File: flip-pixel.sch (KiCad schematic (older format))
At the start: 8 parts, among them Q1 Q_NMOS_DGS, U1 LM2665M6

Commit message: Added charge pump for gate driving, MicroController, and Power Connector
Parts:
- added J?: Barrel-Jack, symbol Custom-Symbols:Barrel-Jack
- added U?: ESP32_DevBoard, symbol Custom-Symbols:ESP32_DevBoard
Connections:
- net labels added: +10V, +5V, Col1H, Col1L, Col2H, Col2L, Col3H, Col3L, Col4H, Col4L, Col5H, Col5L, Row1H, Row1L, Row2H, Row2L, Row3H, Row3L, Row4H, Row4L, Row5H, Row5L
- wire segments 84 -> 157
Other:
- note added: "(AC -> DC Wall Adapter)\nExpects 5V, 2A max rating"
- note added: "Mates With:"
- moved on the sheet: C1, C2, C3, D1, R1, R2, U1

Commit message: Started work on layout
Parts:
- removed Q1: Q_NMOS_DGS, symbol Device:Q_NMOS_DGS
- added D52, D53: LED_Green, LED_SMD:LED_0805_2012Metric_Pad1.15x1.40mm_HandSolder, symbol Custom-Symbols:LED_Green
- added Q1: DMN62D0U-7, Package_TO_SOT_SMD:SOT-23, symbol Custom-Symbols:DMN62D0U-7
- added R23, R24: R, Resistor_SMD:R_0805_2012Metric, symbol Device:R
- C1, C2, C3: footprint (none) -> Capacitor_SMD:C_0805_2012Metric
- R1, R2: footprint (none) -> Resistor_SMD:R_0805_2012Metric
- gave numbers to parts that had none: 2
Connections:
- wire segments 157 -> 163
- no-connect marks 0 -> 10
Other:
- note added: "enable signal enables the high current\noperation of the pixel matrix by\ndriving the charge pump's\nshutdown pin low"
- note removed: "Signal enables the high current\noperation of the pixel matrix by\ndriving the charge pump's\nshutdown pin low"
- moved on the sheet: R1, U2

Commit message: Traces Routed for Charge Pump
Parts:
- J1: footprint (none) -> Connector_BarrelJack:BarrelJack_Horizontal
- U2: footprint (none) -> Custom-Footprints:DIP-38_900_ELL
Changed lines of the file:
@@
 F 0 "U2" H 1650 5465 50  0000 C CNN
 F 1 "ESP32_DevBoard" H 1650 5374 50  0000 C CNN
-F 2 "" H 2000 5450 50  0001 C CNN
+F 2 "Custom-Footprints:DIP-38_900_ELL" H 2000 5450 50  0001 C CNN
 F 3 "http://wiki.ai-thinker.com/_media/esp32/docs/nodemcu-32s_product_specification.pdf" H 2000 5450 50  0001 C CNN
 F 4 "https://www.espressif.com/sites/default/files/documentation/esp32-wroom-32_datasheet_en.pdf" H 1650 4450 50  0001 C CNN "ChipDatasheet"
@@
 F 0 "J1" H 1100 1550 50  0000 C CNN
 F 1 "Barrel-Jack" H 1400 1550 50  0000 C CNN
-F 2 "" H 1700 1550 50  0001 C CNN
+F 2 "Connector_BarrelJack:BarrelJack_Horizontal" H 1700 1550 50  0001 C CNN
 F 3 "https://www.cuidevices.com/product/resource/pj-102b.pdf" H 1700 1550 50  0001 C CNN
 F 4 "Digikey" H 950 2000 50  0001 C CNN "Vendor"

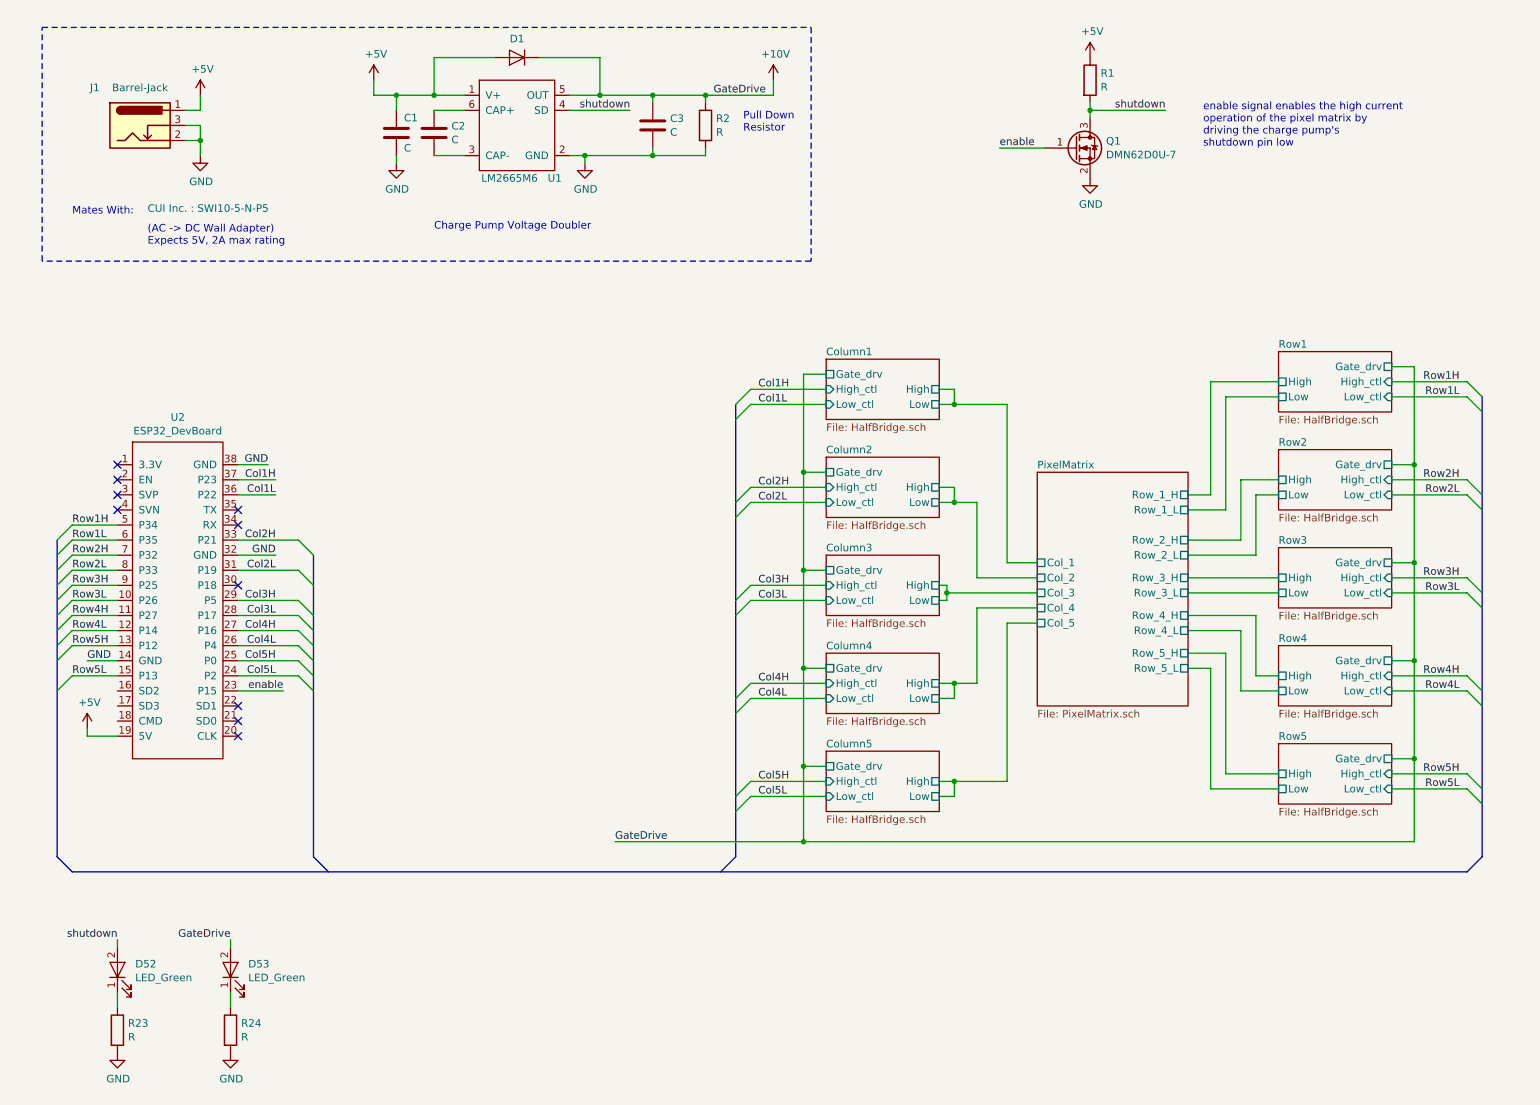
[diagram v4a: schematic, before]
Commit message: Added Current Sensor to Schematic
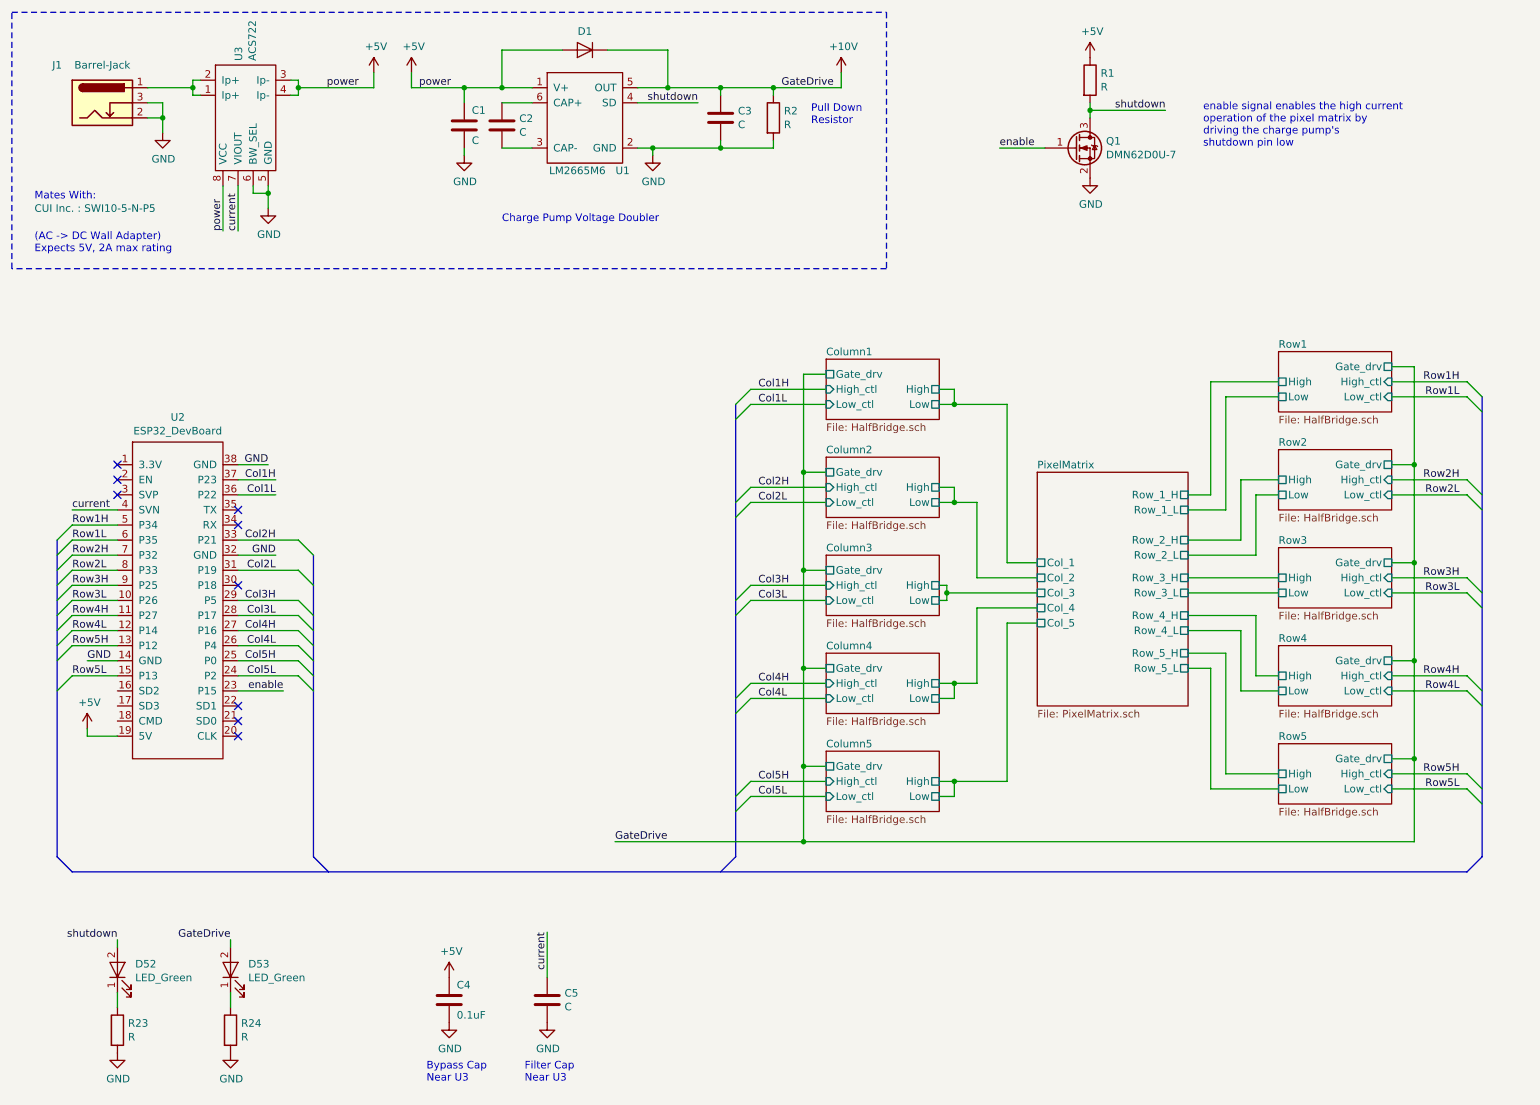
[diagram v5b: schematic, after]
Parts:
- added C4: 0.1uF, Capacitor_SMD:C_0805_2012Metric, symbol Device:C
- added C5: C, Capacitor_SMD:C_0805_2012Metric, symbol Device:C
- added U3: ACS722, Custom-Footprints:SO-8_3.9x4.9mm_P1.27mm, symbol Custom-Symbols:ACS722
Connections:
- net +5V: now also C4.1, U3.3 (Ip-), U3.4 (Ip-), U3.8 (VCC); no longer J1.1
- net GND: now also C4.2, C5.2, U3.5 (GND), U3.6 (BW_SEL)
- net current: now reaches U2.4 (SVN)
- net current: now also C5.1, U3.7 (VIOUT)
- new net: J1.1, U3.1 (Ip+), U3.2 (Ip+)
- no-connect marks 10 -> 9
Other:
- note added: "Bypass Cap\nNear U3"
- note added: "Filter Cap\nNear U3"
- moved on the sheet: C1, C2, C3, D1, J1, R2, U1

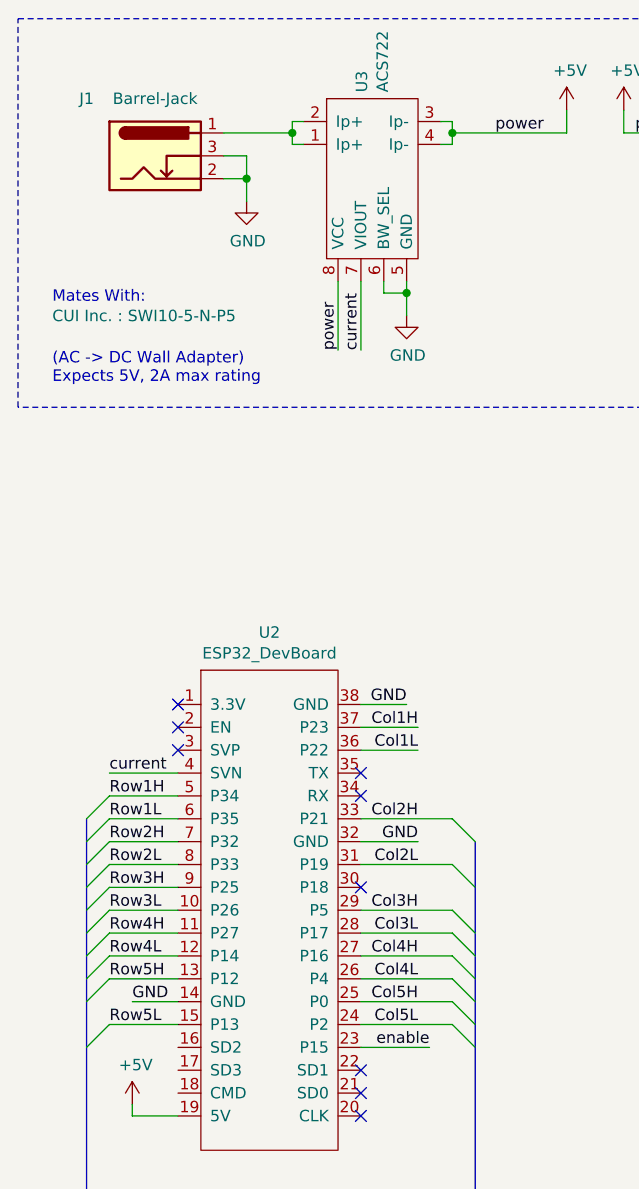
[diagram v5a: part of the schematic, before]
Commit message: Updated Pins to match routes
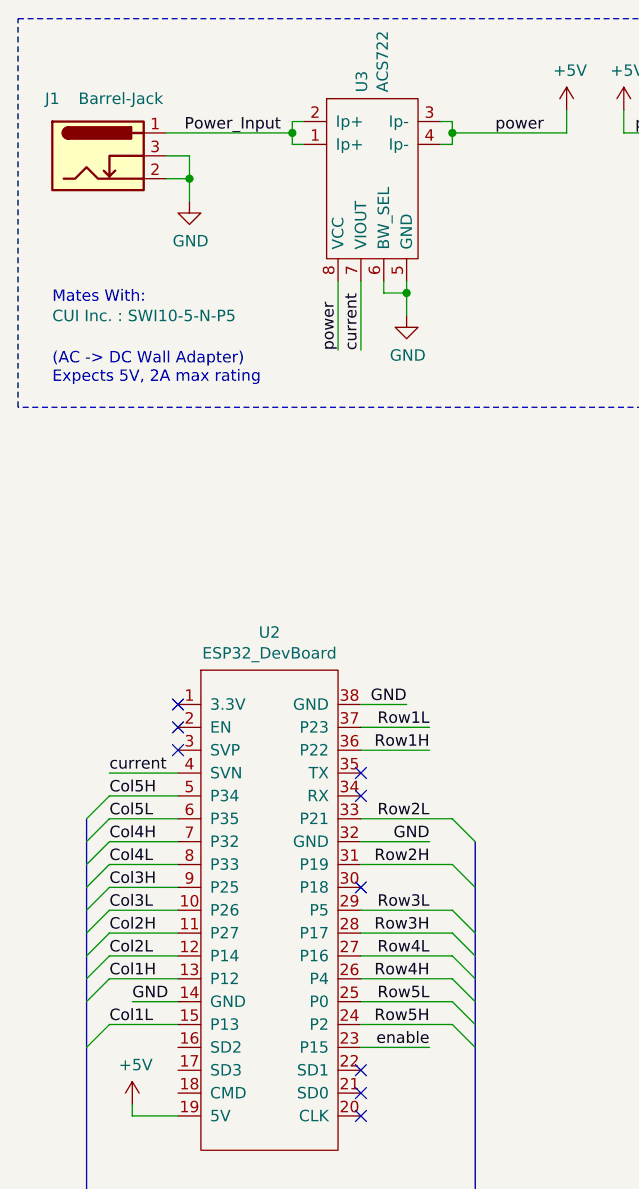
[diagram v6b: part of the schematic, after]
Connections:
- net Col1H: now also U2.13 (P12); no longer U2.37 (P23)
- net Col1L: now also U2.15 (P13); no longer U2.36 (P22)
- net Col2H: now also U2.11 (P27); no longer U2.33 (P21)
- net Col2L: now also U2.12 (P14); no longer U2.31 (P19)
- net Col3H: now also U2.9 (P25); no longer U2.29 (P5)
- net Col3L: now also U2.10 (P26); no longer U2.28 (P17)
- net Col4H: now also U2.7 (P32); no longer U2.27 (P16)
- net Col4L: now also U2.8 (P33); no longer U2.26 (P4)
- net Col5H: now also U2.5 (P34); no longer U2.25 (P0)
- net Col5L: now also U2.6 (P35); no longer U2.24 (P2)
- net Row1H: now also U2.36 (P22); no longer U2.5 (P34)
- net Row1L: now also U2.37 (P23); no longer U2.6 (P35)
- net Row2H: now also U2.31 (P19); no longer U2.7 (P32)
- net Row2L: now also U2.33 (P21); no longer U2.8 (P33)
- net Row3H: now also U2.28 (P17); no longer U2.9 (P25)
- net Row3L: now also U2.29 (P5); no longer U2.10 (P26)
- net Row4H: now also U2.26 (P4); no longer U2.11 (P27)
- net Row4L: now also U2.27 (P16); no longer U2.12 (P14)
- net Row5H: now also U2.24 (P2); no longer U2.13 (P12)
- net Row5L: now also U2.25 (P0); no longer U2.15 (P13)
- net Power_Input: now reaches J1.1, U3.1 (Ip+), U3.2 (Ip+)
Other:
- moved on the sheet: J1
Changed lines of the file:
@@
 $EndComp
 Wire Wire Line
-	2050 3750 2300 3750
-Wire Wire Line
-	2050 3650 2300 3650
+	2050 3750 2350 3750
+Wire Wire Line
+	2050 3650 2350 3650
 Wire Wire Line
 	2050 4050 2450 4050
@@
 Wire Wire Line
 	2050 4850 2450 4850
-Text Label 2300 3650 2    50   ~ 0
+Text Label 2350 3650 2    50   ~ 0
+Row1L
+Text Label 2350 3750 2    50   ~ 0
+Row1H
+Text Label 2350 4050 2    50   ~ 0
+Row2L
+Text Label 2350 4250 2    50   ~ 0
+Row2H
+Text Label 2350 4450 2    50   ~ 0
+Row3L
+Text Label 2350 4550 2    50   ~ 0
+Row3H
+Text Label 2350 4750 2    50   ~ 0
+Row4H
+Text Label 2350 4650 2    50   ~ 0
+Row4L
+Text Label 2350 4850 2    50   ~ 0
+Row5L
+Wire Wire Line
+	1250 3950 950  3950
+Wire Wire Line
+	1250 4050 950  4050
+Wire Wire Line
+	1250 4150 950  4150
+Wire Wire Line
+	1250 4250 950  4250
+Wire Wire Line
+	1250 4350 950  4350
+Wire Wire Line
+	1250 4450 950  4450
+Wire Wire Line
+	1250 4550 950  4550
+Wire Wire Line
+	1250 4650 950  4650
+Wire Wire Line
+	1250 4750 950  4750
+Wire Wire Line
+	1250 4950 950  4950
+Wire Wire Line
+	2050 4950 2450 4950
+Text Label 2350 4950 2    50   ~ 0
+Row5H
+Text Label 950  3950 0    50   ~ 0
+Col5H
+Text Label 950  4050 0    50   ~ 0
+Col5L
+Text Label 950  4150 0    50   ~ 0
+Col4H
+Text Label 950  4250 0    50   ~ 0
+Col4L
+Text Label 950  4350 0    50   ~ 0
+Col3H
+Text Label 950  4450 0    50   ~ 0
+Col3L
+Text Label 950  4550 0    50   ~ 0
+Col2H
+Text Label 950  4650 0    50   ~ 0
+Col2L
+Text Label 950  4750 0    50   ~ 0
 Col1H
-Text Label 2300 3750 2    50   ~ 0
+Text Label 950  4950 0    50   ~ 0
 Col1L
-Text Label 2300 4050 2    50   ~ 0
-Col2H
-Text Label 2300 4250 2    50   ~ 0
-Col2L
-Text Label 2300 4450 2    50   ~ 0
-Col3H
-Text Label 2300 4550 2    50   ~ 0
-Col3L
-Text Label 2300 4650 2    50   ~ 0
-Col4H
-Text Label 2300 4750 2    50   ~ 0
-Col4L
-Text Label 2300 4850 2    50   ~ 0
-Col5H
-Wire Wire Line
-	1250 3950 950  3950
-Wire Wire Line
-	1250 4050 950  4050
-Wire Wire Line
-	1250 4150 950  4150
-Wire Wire Line
-	1250 4250 950  4250
-Wire Wire Line
-	1250 4350 950  4350
-Wire Wire Line
-	1250 4450 950  4450
-Wire Wire Line
-	1250 4550 950  4550
-Wire Wire Line
-	1250 4650 950  4650
-Wire Wire Line
-	1250 4750 950  4750
-Wire Wire Line
-	1250 4950 950  4950
-Wire Wire Line
-	2050 4950 2450 4950
-Text Label 2300 4950 2    50   ~ 0
-Col5L
-Text Label 950  3950 0    50   ~ 0
-Row1H
-Text Label 950  4050 0    50   ~ 0
-Row1L
-Text Label 950  4150 0    50   ~ 0
-Row2H
-Text Label 950  4250 0    50   ~ 0
-Row2L
-Text Label 950  4350 0    50   ~ 0
-Row3H
-Text Label 950  4450 0    50   ~ 0
-Row3L
-Text Label 950  4550 0    50   ~ 0
-Row4H
-Text Label 950  4650 0    50   ~ 0
-Row4L
-Text Label 950  4750 0    50   ~ 0
-Row5H
-Text Label 950  4950 0    50   ~ 0
-Row5L
 Entry Wire Line
 	2450 4050 2550 4150
@@
 L Custom-Symbols:Barrel-Jack J1
 U 1 1 5F1AEA64
-P 1150 1150
-F 0 "J1" H 850 1400 50  0000 C CNN
-F 1 "Barrel-Jack" H 1150 1400 50  0000 C CNN
-F 2 "Connector_BarrelJack:BarrelJack_Horizontal" H 1450 1400 50  0001 C CNN
-F 3 "https://www.cuidevices.com/product/resource/pj-102b.pdf" H 1450 1400 50  0001 C CNN
-F 4 "Digikey" H 700 1850 50  0001 C CNN "Vendor"
-F 5 "CP-102B-ND" H 800 1650 50  0001 C CNN "Vendor Part"
-F 6 "CUI Devices" H 800 1750 50  0001 C CNN "Manufacturer"
-F 7 "CONN PWR JACK 2.5X5.5MM SOLDER" H 1250 1550 50  0001 C CNN "Manufacturer Part"
+P 900 1150
+F 0 "J1" H 700 1400 50  0000 C CNN
+F 1 "Barrel-Jack" H 1000 1400 50  0000 C CNN
+F 2 "Connector_BarrelJack:BarrelJack_Horizontal" H 1200 1400 50  0001 C CNN
+F 3 "https://www.cuidevices.com/product/resource/pj-102b.pdf" H 1200 1400 50  0001 C CNN
+F 4 "Digikey" H 450 1850 50  0001 C CNN "Vendor"
+F 5 "CP-102B-ND" H 550 1650 50  0001 C CNN "Vendor Part"
+F 6 "CUI Devices" H 550 1750 50  0001 C CNN "Manufacturer"
+F 7 "CONN PWR JACK 2.5X5.5MM SOLDER" H 1000 1550 50  0001 C CNN "Manufacturer Part"
 F 8 "CUI Inc. : SWI10-5-N-P5" H 700 450 50  0000 L CNN "Mates With"
-	1    1150 1150
-	1    0    0    -1
-$EndComp
-Wire Wire Line
-	1450 1250 1550 1250
-Wire Wire Line
-	1550 1250 1550 1350
-Wire Wire Line
-	1450 1150 1550 1150
-Wire Wire Line
-	1550 1150 1550 1250
-Connection ~ 1550 1250
+	1    900  1150
+	1    0    0    -1
+$EndComp
+Wire Wire Line
+	1200 1150 1300 1150
 $Comp
 L power:GND #PWR037
 U 1 1 5F1DFED8
-P 1550 1350
-F 0 "#PWR037" H 1550 1100 50  0001 C CNN
-F 1 "GND" H 1555 1177 50  0000 C CNN
-F 2 "" H 1550 1350 50  0001 C CNN
-F 3 "" H 1550 1350 50  0001 C CNN
-	1    1550 1350
+P 1300 1350
+F 0 "#PWR037" H 1300 1100 50  0001 C CNN
+F 1 "GND" H 1305 1177 50  0000 C CNN
+F 2 "" H 1300 1350 50  0001 C CNN
+F 3 "" H 1300 1350 50  0001 C CNN
+	1    1300 1350
 	1    0    0    -1
 $EndComp
@@
 	2000 7050 2000 7150
 Wire Wire Line
-	2050 4150 2300 4150
-Text Label 2300 4150 2    50   ~ 0
+	2050 4150 2350 4150
+Text Label 2350 4150 2    50   ~ 0
 GND
 Text Label 1050 4850 0    50   ~ 0
@@
 	2950 1050 2950 950
 Wire Wire Line
-	1450 1050 1750 1050
+	1200 1050 1750 1050
 $Comp
 L power:+5V #PWR0101
@@
 Text Notes 3300 7650 0    50   ~ 0
 Bypass Cap\nNear U3
+Text Notes 3950 7650 0    50   ~ 0
+Filter Cap\nNear U3
+Text Label 1700 1050 2    50   ~ 0
+Power_Input
+Wire Wire Line
+	1300 1150 1300 1250
+Wire Wire Line
+	1200 1250 1300 1250
 Wire Bus Line
 	950  6250 10200 6250
@@
 Wire Bus Line
 	10300 3100 10300 6150
-Text Notes 3950 7650 0    50   ~ 0
-Filter Cap\nNear U3
+Connection ~ 1300 1250
+Wire Wire Line
+	1300 1250 1300 1350
 $EndSCHEMATC

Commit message: switched to new current sensor
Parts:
- removed U3: ACS722, Custom-Footprints:SO-8_3.9x4.9mm_P1.27mm, symbol Custom-Symbols:ACS722
- added U?: INA250A3, Package_SO:TSSOP-16_4.4x5mm_P0.65mm, symbol Custom-Symbols:INA250A3
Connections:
- net +5V: now also U?.1 (IN-), U?.2 (IN-), U?.3 (IN-)
- net GND: now also U?.11 (GND), U?.6 (GND), U?.7 (REF), U?.8 (GND)
- net Power_Input: now also U?.10 (VS), U?.14 (IN+), U?.15 (IN+), U?.16 (IN+)
- net current: now also U?.9 (OUT)
- new net: U?.12 (VIN+), U?.13 (SH+)
- new net: U?.4 (SH-), U?.5 (VIN-)
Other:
- moved on the sheet: C1, C2, C3, D1, Q1, R1, R2, U1
